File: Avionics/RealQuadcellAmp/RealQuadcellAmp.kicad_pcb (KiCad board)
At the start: 2 copper layers, 115 x 90.5 mm, 46 parts, among them U1 OPA1642AID, U2 OPA1642AID, U3 OPA1642AID, U4 OPA1642AID

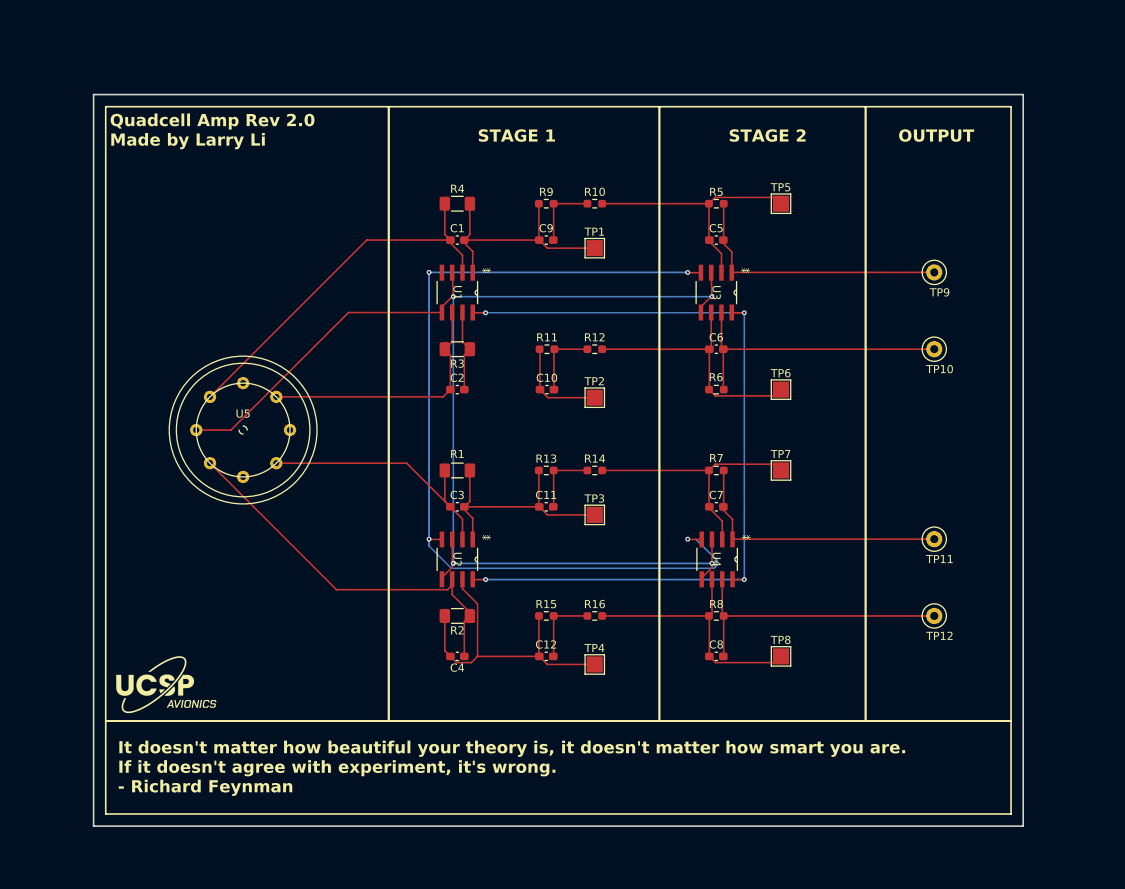
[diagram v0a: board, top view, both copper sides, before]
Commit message: added voltage divider and adjusted routing of quadcell
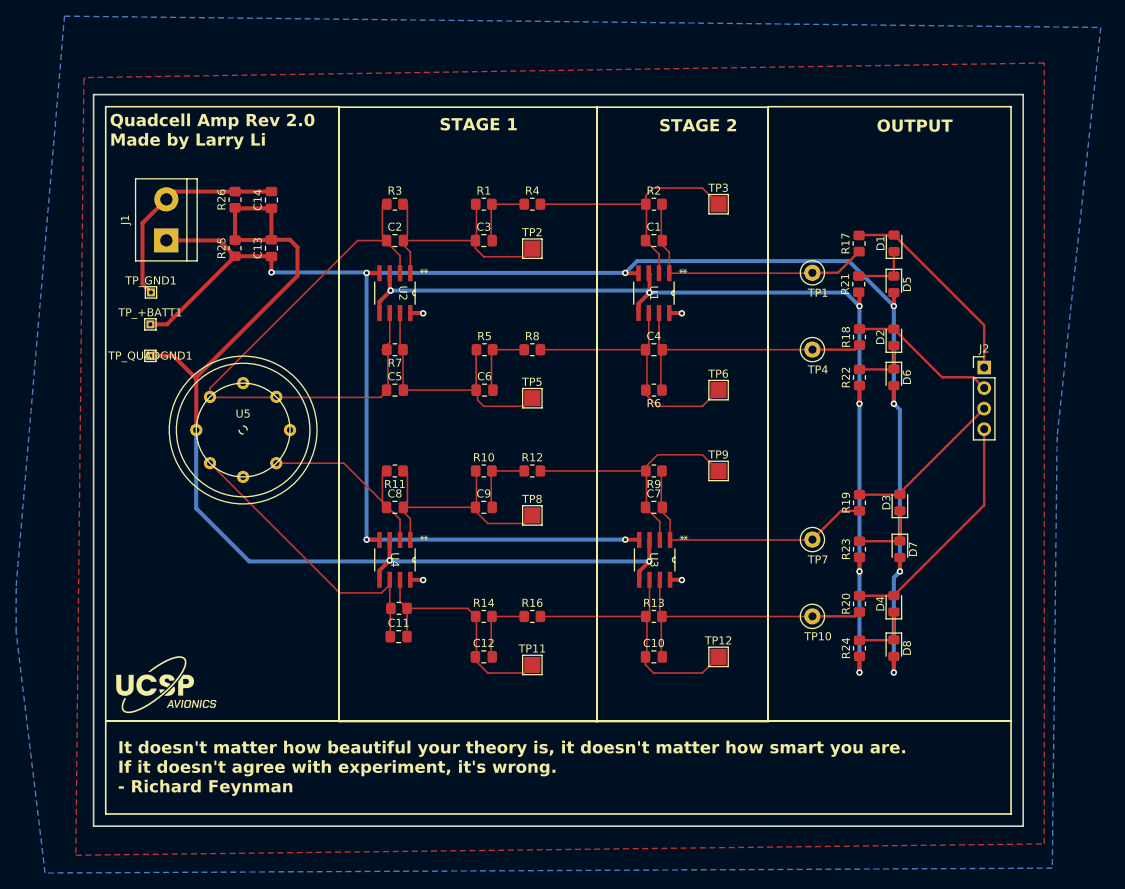
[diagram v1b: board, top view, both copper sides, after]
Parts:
- added C13: 220µF, Capacitor_SMD:C_0805_2012Metric_Pad1.18x1.45mm_HandSolder, F.Cu at (106.0, 58.5)
- added C14: 220µF, Capacitor_SMD:C_0805_2012Metric_Pad1.18x1.45mm_HandSolder, F.Cu at (106.0, 52.5)
- added D1: ~, Diode_SMD:D_0805_2012Metric_Pad1.15x1.40mm_HandSolder, F.Cu at (183.0, 57.9)
- added D2: ~, Diode_SMD:D_0805_2012Metric_Pad1.15x1.40mm_HandSolder, F.Cu at (183.0, 69.5)
- added D3: ~, Diode_SMD:D_0805_2012Metric_Pad1.15x1.40mm_HandSolder, F.Cu at (183.8, 90.0)
- added D4: ~, Diode_SMD:D_0805_2012Metric_Pad1.15x1.40mm_HandSolder, F.Cu at (183.0, 102.5)
- added D5: ~, Diode_SMD:D_0805_2012Metric_Pad1.15x1.40mm_HandSolder, F.Cu at (183.0, 63.0)
- added D6: ~, Diode_SMD:D_0805_2012Metric_Pad1.15x1.40mm_HandSolder, F.Cu at (183.0, 74.5)
- added D7: ~, Diode_SMD:D_0805_2012Metric_Pad1.15x1.40mm_HandSolder, F.Cu at (183.8, 95.8)
- added D8: ~, Diode_SMD:D_0805_2012Metric_Pad1.15x1.40mm_HandSolder, F.Cu at (183.0, 108.0)
- added J1: Screw_Terminal_01x02, TerminalBlock:TerminalBlock_bornier-2_P5.08mm, F.Cu at (93.0, 57.5)
- added J2: Conn_01x04_Pin, Connector_PinHeader_2.54mm:PinHeader_1x04_P2.54mm_Vertical, F.Cu at (194.2, 73.3)
- added R17: 1 kΩ, Resistor_SMD:R_0805_2012Metric_Pad1.20x1.40mm_HandSolder, F.Cu at (178.7, 57.9)
- added R18: 1 kΩ, Resistor_SMD:R_0805_2012Metric_Pad1.20x1.40mm_HandSolder, F.Cu at (178.8, 69.5)
- added R19: 1 kΩ, Resistor_SMD:R_0805_2012Metric_Pad1.20x1.40mm_HandSolder, F.Cu at (178.8, 90.0)
- added R20: 1 kΩ, Resistor_SMD:R_0805_2012Metric_Pad1.20x1.40mm_HandSolder, F.Cu at (178.8, 102.5)
- added R21: 40 Ω, Resistor_SMD:R_0805_2012Metric_Pad1.20x1.40mm_HandSolder, F.Cu at (178.7, 63.0)
- added R22: 40 Ω, Resistor_SMD:R_0805_2012Metric_Pad1.20x1.40mm_HandSolder, F.Cu at (178.8, 74.5)
- added R23: 40 Ω, Resistor_SMD:R_0805_2012Metric_Pad1.20x1.40mm_HandSolder, F.Cu at (178.8, 95.8)
- added R24: 40 Ω, Resistor_SMD:R_0805_2012Metric_Pad1.20x1.40mm_HandSolder, F.Cu at (178.8, 108.0)
- added R25: 4.7k, Resistor_SMD:R_0805_2012Metric_Pad1.20x1.40mm_HandSolder, F.Cu at (101.5, 58.5)
- added R26: 4.7k, Resistor_SMD:R_0805_2012Metric_Pad1.20x1.40mm_HandSolder, F.Cu at (101.5, 52.5)
- added TP_+BATT1: TestPoint, TestPoint:TestPoint_THTPad_1.0x1.0mm_Drill0.5mm, F.Cu at (91.0, 67.9)
- added TP_GND1: TestPoint, TestPoint:TestPoint_THTPad_1.0x1.0mm_Drill0.5mm, F.Cu at (91.1, 64.0)
- added TP_QUADGND1: TestPoint, TestPoint:TestPoint_THTPad_1.0x1.0mm_Drill0.5mm, F.Cu at (91.0, 71.8)
- C1: renamed from C5; footprint Capacitor_SMD:C_0603_1608Metric_Pad1.08x0.95mm_HandSolder -> Capacitor_SMD:C_0805_2012Metric_Pad1.18x1.45mm_HandSolder
- C10: renamed from C8; footprint Capacitor_SMD:C_0603_1608Metric_Pad1.08x0.95mm_HandSolder -> Capacitor_SMD:C_0805_2012Metric_Pad1.18x1.45mm_HandSolder
- C11: renamed from C4; value 10 pf -> 5 pf; footprint Capacitor_SMD:C_0603_1608Metric_Pad1.08x0.95mm_HandSolder -> Capacitor_SMD:C_0805_2012Metric_Pad1.18x1.45mm_HandSolder
- C12, C7: footprint Capacitor_SMD:C_0603_1608Metric_Pad1.08x0.95mm_HandSolder -> Capacitor_SMD:C_0805_2012Metric_Pad1.18x1.45mm_HandSolder
- C2: renamed from C1; value 10 pf -> 5 pf; footprint Capacitor_SMD:C_0603_1608Metric_Pad1.08x0.95mm_HandSolder -> Capacitor_SMD:C_0805_2012Metric_Pad1.18x1.45mm_HandSolder
- C3: renamed from C9; footprint Capacitor_SMD:C_0603_1608Metric_Pad1.08x0.95mm_HandSolder -> Capacitor_SMD:C_0805_2012Metric_Pad1.18x1.45mm_HandSolder
- C4: renamed from C6; footprint Capacitor_SMD:C_0603_1608Metric_Pad1.08x0.95mm_HandSolder -> Capacitor_SMD:C_0805_2012Metric_Pad1.18x1.45mm_HandSolder
- C5: renamed from C2; value 10 pf -> 5 pf; footprint Capacitor_SMD:C_0603_1608Metric_Pad1.08x0.95mm_HandSolder -> Capacitor_SMD:C_0805_2012Metric_Pad1.18x1.45mm_HandSolder
- C6: renamed from C10; footprint Capacitor_SMD:C_0603_1608Metric_Pad1.08x0.95mm_HandSolder -> Capacitor_SMD:C_0805_2012Metric_Pad1.18x1.45mm_HandSolder
- C8: renamed from C3; value 10 pf -> 5 pf; footprint Capacitor_SMD:C_0603_1608Metric_Pad1.08x0.95mm_HandSolder -> Capacitor_SMD:C_0805_2012Metric_Pad1.18x1.45mm_HandSolder
- C9: renamed from C11; footprint Capacitor_SMD:C_0603_1608Metric_Pad1.08x0.95mm_HandSolder -> Capacitor_SMD:C_0805_2012Metric_Pad1.18x1.45mm_HandSolder
- R1: renamed from R9; value 0.1 MΩ -> 68.1 kΩ; footprint Resistor_SMD:R_0603_1608Metric_Pad0.98x0.95mm_HandSolder -> Resistor_SMD:R_0805_2012Metric_Pad1.20x1.40mm_HandSolder
- R10: renamed from R13; value 0.1 MΩ -> 68.1 kΩ; footprint Resistor_SMD:R_0603_1608Metric_Pad0.98x0.95mm_HandSolder -> Resistor_SMD:R_0805_2012Metric_Pad1.20x1.40mm_HandSolder
- R11: renamed from R1; value 1 GΩ -> 100 MΩ; footprint Resistor_SMD:R_1206_3216Metric_Pad1.30x1.75mm_HandSolder -> Resistor_SMD:R_0805_2012Metric_Pad1.20x1.40mm_HandSolder
- R12: renamed from R14; value 33.1 kΩ -> 38.1 kΩ; footprint Resistor_SMD:R_0603_1608Metric_Pad0.98x0.95mm_HandSolder -> Resistor_SMD:R_0805_2012Metric_Pad1.20x1.40mm_HandSolder
- R13: renamed from R8; value 1.34 MΩ -> 15 MΩ; footprint Resistor_SMD:R_0603_1608Metric_Pad0.98x0.95mm_HandSolder -> Resistor_SMD:R_0805_2012Metric_Pad1.20x1.40mm_HandSolder
- R14: renamed from R15; value 0.1 MΩ -> 68.1 kΩ; footprint Resistor_SMD:R_0603_1608Metric_Pad0.98x0.95mm_HandSolder -> Resistor_SMD:R_0805_2012Metric_Pad1.20x1.40mm_HandSolder
- R15: renamed from R2; value 1 GΩ -> 100 MΩ; footprint Resistor_SMD:R_1206_3216Metric_Pad1.30x1.75mm_HandSolder -> Resistor_SMD:R_0805_2012Metric_Pad1.20x1.40mm_HandSolder
- R16: value 33.1 kΩ -> 38.1 kΩ; footprint Resistor_SMD:R_0603_1608Metric_Pad0.98x0.95mm_HandSolder -> Resistor_SMD:R_0805_2012Metric_Pad1.20x1.40mm_HandSolder
- R2: renamed from R5; value 1.34 MΩ -> 15 MΩ; footprint Resistor_SMD:R_0603_1608Metric_Pad0.98x0.95mm_HandSolder -> Resistor_SMD:R_0805_2012Metric_Pad1.20x1.40mm_HandSolder
- R3: renamed from R4; value 1 GΩ -> 100 MΩ; footprint Resistor_SMD:R_1206_3216Metric_Pad1.30x1.75mm_HandSolder -> Resistor_SMD:R_0805_2012Metric_Pad1.20x1.40mm_HandSolder
- R4: renamed from R10; value 33.1 kΩ -> 38.1 kΩ; footprint Resistor_SMD:R_0603_1608Metric_Pad0.98x0.95mm_HandSolder -> Resistor_SMD:R_0805_2012Metric_Pad1.20x1.40mm_HandSolder
- R5: renamed from R11; value 0.1 MΩ -> 68.1 kΩ; footprint Resistor_SMD:R_0603_1608Metric_Pad0.98x0.95mm_HandSolder -> Resistor_SMD:R_0805_2012Metric_Pad1.20x1.40mm_HandSolder
- R6: value 1.34 MΩ -> 15 MΩ; footprint Resistor_SMD:R_0603_1608Metric_Pad0.98x0.95mm_HandSolder -> Resistor_SMD:R_0805_2012Metric_Pad1.20x1.40mm_HandSolder
- R7: renamed from R3; value 1 GΩ -> 100 MΩ; footprint Resistor_SMD:R_1206_3216Metric_Pad1.30x1.75mm_HandSolder -> Resistor_SMD:R_0805_2012Metric_Pad1.20x1.40mm_HandSolder
- R8: renamed from R12; value 33.1 kΩ -> 38.1 kΩ; footprint Resistor_SMD:R_0603_1608Metric_Pad0.98x0.95mm_HandSolder -> Resistor_SMD:R_0805_2012Metric_Pad1.20x1.40mm_HandSolder
- R9: renamed from R7; value 1.34 MΩ -> 15 MΩ; footprint Resistor_SMD:R_0603_1608Metric_Pad0.98x0.95mm_HandSolder -> Resistor_SMD:R_0805_2012Metric_Pad1.20x1.40mm_HandSolder
- moved TP1 15.1 mm to (172.9, 61.5)
- moved TP10 15.1 mm to (172.9, 104.0)
- moved TP4 15.1 mm to (172.9, 71.0)
- moved TP7 15.1 mm to (172.9, 94.5)
- moved C1 7.73 mm to (153.3, 57.6)
- moved C10 7.73 mm to (153.3, 109.1)
- moved C12 7.73 mm to (132.3, 109.1)
- moved C2 7.73 mm to (121.3, 57.6)
- moved C3 7.73 mm to (132.3, 57.6)
- moved C4 7.73 mm to (153.3, 71.1)
- moved C5 7.73 mm to (121.3, 76.1)
- moved C6 7.73 mm to (132.4, 76.1)
- moved C7 7.73 mm to (153.3, 90.6)
- moved C8 7.73 mm to (121.3, 90.6)
- moved C9 7.73 mm to (132.3, 90.6)
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- renumbered TP9 to TP1, TP12 to TP10, TP4 to TP11, TP8 to TP12, TP1 to TP2, TP5 to TP3, TP10 to TP4, TP2 to TP5, TP11 to TP7, TP3 to TP8, TP7 to TP9, U3 to U1, U1 to U2, U4 to U3, U2 to U4
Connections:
- U1 pad 3: GND -> QUAD_GND
- U1 pad 5: GND -> QUAD_GND
- U1 pad 8: VEE -> GND
- U2 pad 3: GND -> QUAD_GND
- U2 pad 5: GND -> QUAD_GND
- U2 pad 8: VEE -> GND
- U3 pad 3: GND -> QUAD_GND
- U3 pad 5: GND -> QUAD_GND
- U3 pad 8: VEE -> GND
- U4 pad 3: GND -> QUAD_GND
- U4 pad 5: GND -> QUAD_GND
- U4 pad 8: VEE -> GND
- U5 pad 0: GND -> QUAD_GND
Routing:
- net QUAD_GND: track 0.00 -> 262.5 mm, vias 0 -> 8
- net GND: track 156.3 -> 33.0 mm
- net VCC: track 113.3 -> 236.2 mm, vias 4 -> 9
- net VEE: track 103.3 -> 0.00 mm, vias 4 -> 0
- net /FOUT4: track 0.00 -> 29.5 mm
- net /FOUT1: track 0.00 -> 25.4 mm
- net /FOUT3: track 0.00 -> 19.9 mm
- net /FOUT2: track 0.00 -> 18.5 mm
- net /IN4: track 48.1 -> 37.0 mm
- net Net-(U2-OUTB): track 22.4 -> 32.5 mm
- net Net-(U4-OUTB): track 39.5 -> 30.3 mm
- net Net-(D3-K): track 0.00 -> 8.74 mm
- net /IN3: track 33.2 -> 25.5 mm
- net Net-(D4-K): track 0.00 -> 7.70 mm
- net Net-(D1-K): track 0.00 -> 7.39 mm
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- added copper zone on B.Cu, net GND
- added copper zone on F.Cu, net GND

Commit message: small tweak from previous push
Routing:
- net QUAD_GND: track 262.5 -> 295.8 mm
- removed copper zone on F.Cu, net GND
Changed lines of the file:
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@@
+	)
+	(segment
+		(start 152.75 97.25)
+		(end 152.75 64.025)
+		(width 0.5)
+		(layer "B.Cu")
+		(net 20)
 	)
 	(segment
@@
 		(start 178.75 98.5)
 		(end 178.75 111)
+		(width 0.5)
+		(layer "B.Cu")
+		(net 20)
+	)
+	(segment
+		(start 152.75 64.025)
+		(end 152.775 64)
 		(width 0.5)
 		(layer "B.Cu")
@@
 		(net 19)
 		(net_name "GND")
-		(layer "F.Cu")
+		(layer "B.Cu")
 		(hatch edge 0.5)
-		(priority 1)
 		(connect_pads
 			(clearance 0.5)
@@
 		(min_thickness 0.25)
 		(filled_areas_thickness no)
-		(fill
+		(fill yes
 			(thermal_gap 0.5)
 			(thermal_bridge_width 0.5)
@@
 		(polygon
 			(pts
-				(xy 82.8 37.6) (xy 81.8 133.6) (xy 201.6 132.2) (xy 201.6 35.6) (xy 83 37.4)
+				(xy 74.420366 100.299698) (xy 80.4 29.8) (xy 208.6 31.2) (xy 203.2 81.8) (xy 202.6 135.2) (xy 78 135.8)
+				(xy 74.420366 106.049698)
 			)
 		)
@@
 			)
 		)
-	)
-	(zone
-		(net 19)
-		(net_name "GND")
-		(layer "B.Cu")
-		(hatch edge 0.5)
-		(connect_pads
-			(clearance 0.5)
-		)
-		(min_thickness 0.25)
-		(filled_areas_thickness no)
-		(fill yes
-			(thermal_gap 0.5)
-			(thermal_bridge_width 0.5)
-		)
-		(polygon
-			(pts
-				(xy 74.420366 100.299698) (xy 80.4 29.8) (xy 208.6 31.2) (xy 203.2 81.8) (xy 202.6 135.2) (xy 78 135.8)
-				(xy 74.420366 106.049698)
-			)
-		)

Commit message: a few more small tweaks to quadcell
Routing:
- net /IN2: track 32.1 -> 24.4 mm
- net VCC: track 236.2 -> 242.7 mm, vias 9 -> 10
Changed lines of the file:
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@@
 		(tags "test point THT pad rectangle square")
 		(property "Reference" "TP_QUADGND1"
-			(at 0 0 0)
+			(at 0 -1.825 0)
 			(layer "F.SilkS")
 			(effects
@@
 	)
 	(segment
-		(start 119.725 71.0625)
-		(end 119.725 71.1125)
+		(start 120.64 70.1475)
+		(end 120.64 66.5263)
 		(width 0.2)
 		(layer "F.Cu")
@@
 	)
 	(segment
-		(start 120.64 70.1475)
-		(end 120.64 66.5263)
+		(start 119.475 77)
+		(end 120.4125 76.0625)
 		(width 0.2)
 		(layer "F.Cu")
@@
 	(segment
 		(start 119.725 71.1125)
-		(end 120.4125 71.8)
+		(end 119.725 71.0625)
 		(width 0.2)
 		(layer "F.Cu")
@@
 	)
 	(segment
-		(start 120.4125 71.8)
-		(end 120.4125 76.0625)
+		(start 106.8 77)
+		(end 119.475 77)
 		(width 0.2)
 		(layer "F.Cu")
@@
 	)
 	(segment
-		(start 98.876219 76.961281)
-		(end 119.513719 76.961281)
+		(start 120.4125 71.8)
+		(end 119.725 71.1125)
 		(width 0.2)
 		(layer "F.Cu")
@@
 	)
 	(segment
-		(start 119.513719 76.961281)
-		(end 120.4125 76.0625)
+		(start 106.698781 76.898781)
+		(end 106.8 77)
 		(width 0.2)
 		(layer "F.Cu")
@@
 	)
 	(segment
+		(start 106.601219 76.898781)
+		(end 106.698781 76.898781)
+		(width 0.2)
+		(layer "F.Cu")
+		(net 3)
+	)
+	(segment
+		(start 120.4125 76.0625)
+		(end 120.4125 71.8)
+		(width 0.2)
+		(layer "F.Cu")
+		(net 3)
+	)
+	(segment
 		(start 120.4125 90.5625)
 		(end 121.91 92.06)
@@
 	)
 	(segment
+		(start 101.6 59.6)
+		(end 101.5 59.5)
+		(width 0.5)
+		(layer "F.Cu")
+		(net 18)
+	)
+	(segment
 		(start 151.4688 94.5625)
 		(end 151.505 94.5987)
@@
 	)
 	(segment
+		(start 101.6 61.6)
+		(end 101.6 59.6)
+		(width 0.5)
+		(layer "F.Cu")
+		(net 18)
+	)
+	(segment
 		(start 183 65.675)
 		(end 183 64)
@@
 		(net 18)
 	)
+	(via
+		(at 101.6 61.6)
+		(size 0.8)
+		(drill 0.4)
+		(layers "F.Cu" "B.Cu")
+		(free yes)
+		(net 18)
+	)
 	(segment
 		(start 183 77.75)
@@
 	)
 	(segment
+		(start 101.6 61.6)
+		(end 105.9 61.6)
+		(width 0.5)
+		(layer "B.Cu")
+		(net 18)
+	)
+	(segment
 		(start 149.775 61.5625)
 		(end 151.2375 60.1)
@@
 	)
 	(segment
+		(start 105.9 61.6)
+		(end 106 61.5)
+		(width 0.5)
+		(layer "B.Cu")
+		(net 18)
+	)
+	(segment
 		(start 183.75 98.5)
 		(end 183.75 78.5)
@@
 	)
 	(zone
-		(net 19)
-		(net_name "GND")
-		(layer "B.Cu")
-		(hatch edge 0.5)
-		(connect_pads
-			(clearance 0.5)
-		)
-		(min_thickness 0.25)
-		(filled_areas_thickness no)
-		(fill yes
-			(thermal_gap 0.5)
-			(thermal_bridge_width 0.5)
-		)
-		(polygon
-			(pts
-				(xy 74.420366 100.299698) (xy 80.4 29.8) (xy 208.6 31.2) (xy 203.2 81.8) (xy 202.6 135.2) (xy 78 135.8)
-				(xy 74.420366 106.049698)
-			)
-		)
-	)
-	(zone
 		(net 18)
 		(net_name "VCC")
@@
 		(name "$teardrop_padvia$")
 		(hatch full 0.1)
-		(priority 30001)
+		(priority 30000)
 		(attr
 			(teardrop
@@
 		(polygon
 			(pts
-				(xy 118.575 94.8125) (xy 118.575 94.3125) (xy 117.775 94.1625) (xy 117.774 94.5625) (xy 117.775 94.9625)
+				(xy 118.025 93.7625) (xy 117.525 93.7625) (xy 117.375 94.5625) (xy 117.775 94.5635) (xy 118.175 94.5625)
+			)
+		)
+	)
+	(zone
+		(net 19)
+		(net_name "GND")
+		(layer "B.Cu")
+		(hatch edge 0.5)
+		(connect_pads
+			(clearance 0.5)
+		)
+		(min_thickness 0.25)
+		(filled_areas_thickness no)
+		(fill yes
+			(thermal_gap 0.5)
+			(thermal_bridge_width 0.5)
+		)
+		(polygon
+			(pts
+				(xy 74.420366 100.299698) (xy 80.4 29.8) (xy 208.6 31.2) (xy 203.2 81.8) (xy 202.6 135.2) (xy 78 135.8)
+				(xy 74.420366 106.049698)
 			)
 		)
@@
 		(name "$teardrop_padvia$")
 		(hatch full 0.1)
-		(priority 30000)
+		(priority 30001)
 		(attr
 			(teardrop
@@
 		(polygon
 			(pts
-				(xy 118.025 93.7625) (xy 117.525 93.7625) (xy 117.375 94.5625) (xy 117.775 94.5635) (xy 118.175 94.5625)
+				(xy 118.575 94.8125) (xy 118.575 94.3125) (xy 117.775 94.1625) (xy 117.774 94.5625) (xy 117.775 94.9625)
 			)
 		)

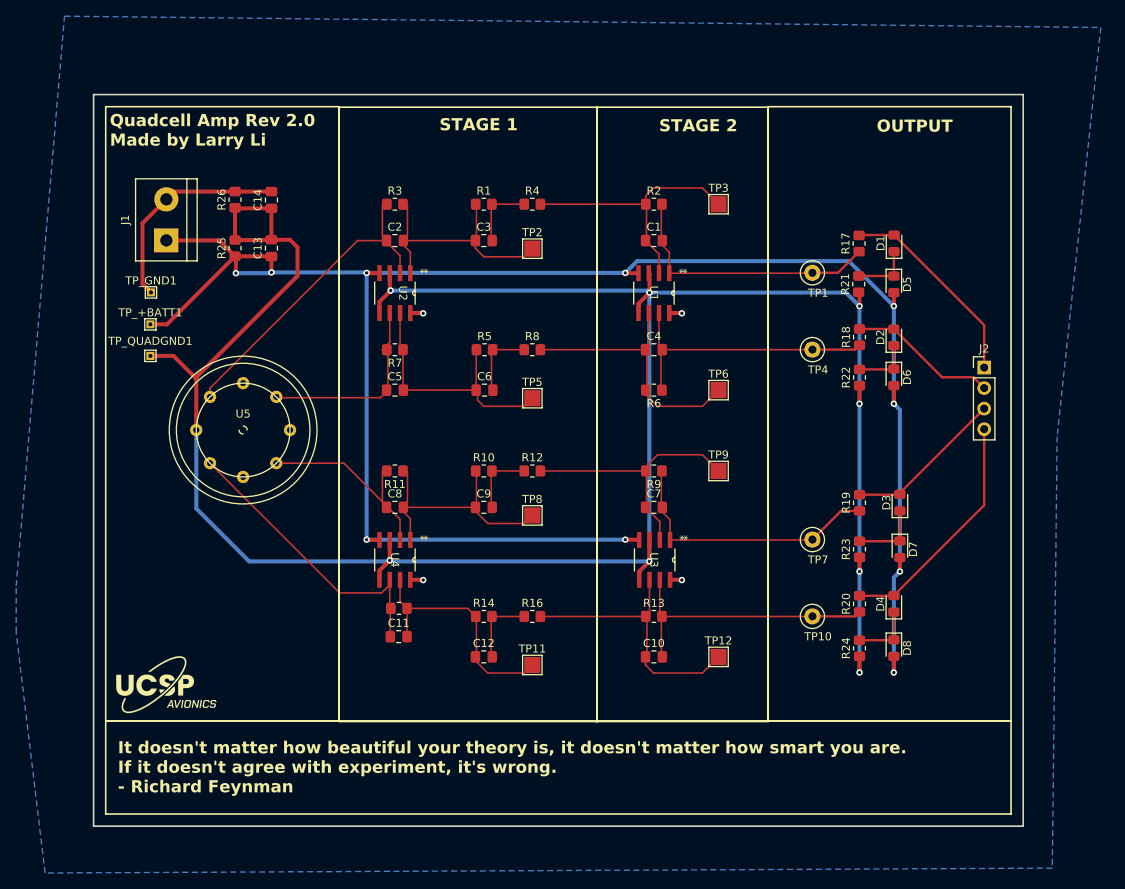
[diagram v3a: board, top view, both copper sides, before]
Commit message: added voltage divider to quadcell
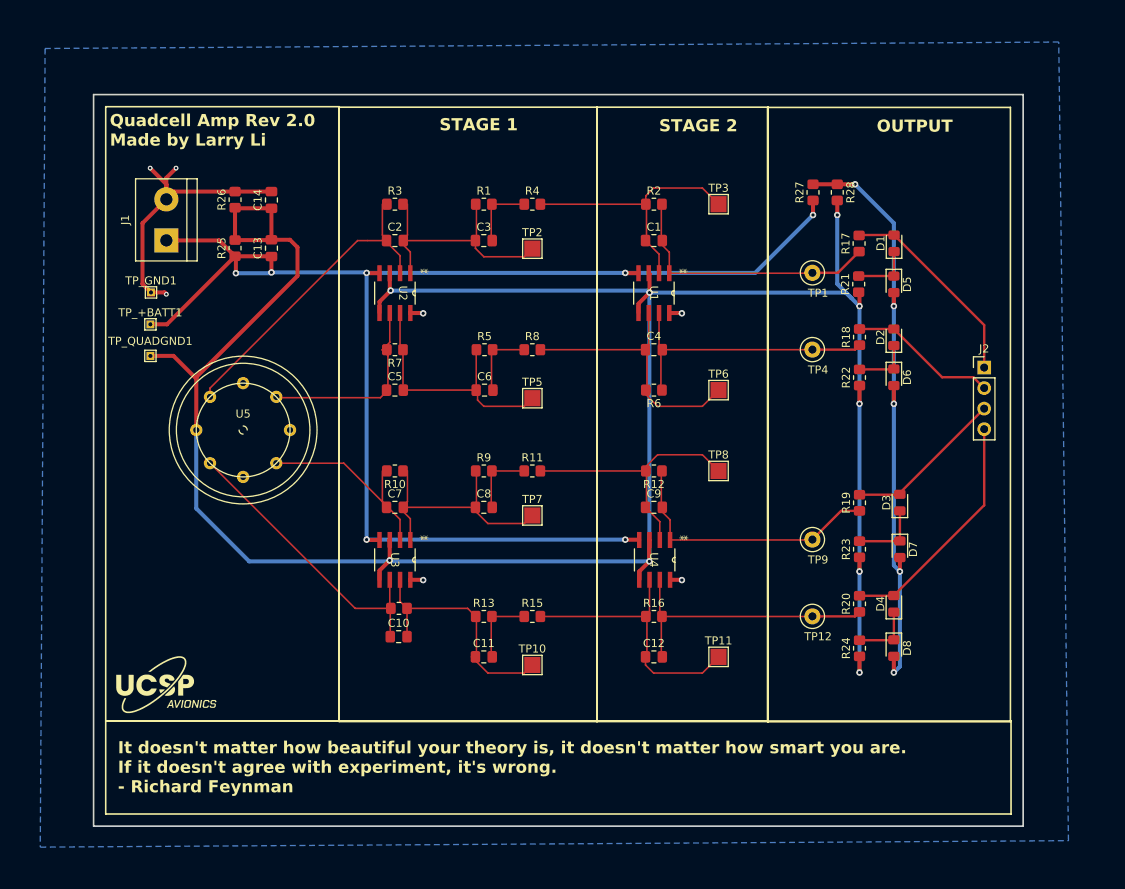
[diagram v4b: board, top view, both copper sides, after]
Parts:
- added R27: 11k, Resistor_SMD:R_0805_2012Metric_Pad1.20x1.40mm_HandSolder, F.Cu at (173.0, 51.6)
- added R28: 29k, Resistor_SMD:R_0805_2012Metric_Pad1.20x1.40mm_HandSolder, F.Cu at (176.0, 51.6)
- renumbered C11 to C10, C12 to C11, C10 to C12, C8 to C7, C9 to C8, C7 to C9, R11 to R10, R12 to R11, R9 to R12, R14 to R13, R15 to R14, R16 to R15, R13 to R16, R10 to R9, TP11 to TP10, TP12 to TP11, TP10 to TP12, TP8 to TP7, TP9 to TP8, TP7 to TP9, U4 to U3, U3 to U4
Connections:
- D5 pad 2: VCC -> +3V3
- D6 pad 2: VCC -> +3V3
- D7 pad 2: VCC -> +3V3
- D8 pad 2: VCC -> +3V3
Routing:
- net +3V3: track 0.00 -> 75.9 mm, vias 0 -> 5
- net VCC: track 242.7 -> 181.0 mm, vias 10 -> 7
- net QUAD_GND: track 295.8 -> 308.6 mm, vias 8 -> 9
- net GND: track 33.0 -> 44.1 mm, vias 4 -> 7
- net /IN4: track 37.0 -> 37.5 mm
